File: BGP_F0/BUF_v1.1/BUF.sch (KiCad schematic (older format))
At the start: 35 parts, among them P1 CONN_01X02, P2 CONN_01X02, P3 CONN_01X03, P4 CONN_01X02, P5 CONN_01X09, P6 CONN_01X05, P7 CONN_01X02, Q1 2N5457, Q2 2N5457, U1 MC33178

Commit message: Some changes to names
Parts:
- C6: value 100p -> 270p
- R10: value 100 -> 1k
- R5, R6: value 49.9k -> 47k
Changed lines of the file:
@@
 $EndComp
 $Comp
-L Earth #PWR4
+L Earth #PWR01
 U 1 1 5A651373
 P 2850 2800
-F 0 "#PWR4" H 2850 2550 50  0001 C CNN
+F 0 "#PWR01" H 2850 2550 50  0001 C CNN
 F 1 "Earth" H 2850 2650 50  0001 C CNN
 F 2 "" H 2850 2800 50  0000 C CNN
@@
 VRef
 $Comp
-L Earth #PWR7
+L Earth #PWR02
 U 1 1 5A653AB7
 P 3800 4350
-F 0 "#PWR7" H 3800 4100 50  0001 C CNN
+F 0 "#PWR02" H 3800 4100 50  0001 C CNN
 F 1 "Earth" H 3800 4200 50  0001 C CNN
 F 2 "" H 3800 4350 50  0000 C CNN
@@
 P 5200 2800
 F 0 "R5" H 5230 2820 50  0000 L CNN
-F 1 "49.9k" H 5230 2760 50  0000 L CNN
+F 1 "47k" H 5230 2760 50  0000 L CNN
 F 2 "Resistors_SMD:R_0603" H 5200 2800 50  0001 C CNN
 F 3 "" H 5200 2800 50  0000 C CNN
@@
 P 5200 3200
 F 0 "R6" H 5230 3220 50  0000 L CNN
-F 1 "49.9k" H 5230 3160 50  0000 L CNN
+F 1 "47k" H 5230 3160 50  0000 L CNN
 F 2 "Resistors_SMD:R_0603" H 5200 3200 50  0001 C CNN
 F 3 "" H 5200 3200 50  0000 C CNN
@@
 $EndComp
 $Comp
-L Earth #PWR8
+L Earth #PWR03
 U 1 1 5A654108
 P 5700 3600
-F 0 "#PWR8" H 5700 3350 50  0001 C CNN
+F 0 "#PWR03" H 5700 3350 50  0001 C CNN
 F 1 "Earth" H 5700 3450 50  0001 C CNN
 F 2 "" H 5700 3600 50  0000 C CNN
@@
 P 5700 4100
 F 0 "C6" H 5710 4170 50  0000 L CNN
-F 1 "100p" H 5710 4020 50  0000 L CNN
+F 1 "270p" H 5710 4020 50  0000 L CNN
 F 2 "Capacitors_SMD:C_0603" H 5700 4100 50  0001 C CNN
 F 3 "" H 5700 4100 50  0000 C CNN
@@
 $EndComp
 $Comp
-L Earth #PWR9
+L Earth #PWR04
 U 1 1 5A6549CA
 P 5700 5400
-F 0 "#PWR9" H 5700 5150 50  0001 C CNN
+F 0 "#PWR04" H 5700 5150 50  0001 C CNN
 F 1 "Earth" H 5700 5250 50  0001 C CNN
 F 2 "" H 5700 5400 50  0000 C CNN
@@
 P 7200 3300
 F 0 "R10" H 7230 3320 50  0000 L CNN
-F 1 "100" H 7230 3260 50  0000 L CNN
+F 1 "1k" H 7230 3260 50  0000 L CNN
 F 2 "Resistors_SMD:R_0603" H 7200 3300 50  0001 C CNN
 F 3 "" H 7200 3300 50  0000 C CNN
@@
 $EndComp
 $Comp
-L Earth #PWR10
+L Earth #PWR05
 U 1 1 5A655780
 P 7650 3900
-F 0 "#PWR10" H 7650 3650 50  0001 C CNN
+F 0 "#PWR05" H 7650 3650 50  0001 C CNN
 F 1 "Earth" H 7650 3750 50  0001 C CNN
 F 2 "" H 7650 3900 50  0000 C CNN
@@
 $EndComp
 $Comp
-L Earth #PWR11
+L Earth #PWR06
 U 1 1 5A6578E9
 P 8350 4800
-F 0 "#PWR11" H 8350 4550 50  0001 C CNN
+F 0 "#PWR06" H 8350 4550 50  0001 C CNN
 F 1 "Earth" H 8350 4650 50  0001 C CNN
 F 2 "" H 8350 4800 50  0000 C CNN
@@
 PV_2
 $Comp
-L Earth #PWR2
+L Earth #PWR07
 U 1 1 5A658545
 P 2600 4000
-F 0 "#PWR2" H 2600 3750 50  0001 C CNN
+F 0 "#PWR07" H 2600 3750 50  0001 C CNN
 F 1 "Earth" H 2600 3850 50  0001 C CNN
 F 2 "" H 2600 4000 50  0000 C CNN
@@
 $EndComp
 $Comp
-L Earth #PWR1
+L Earth #PWR08
 U 1 1 5A6585B9
 P 2600 2600
-F 0 "#PWR1" H 2600 2350 50  0001 C CNN
+F 0 "#PWR08" H 2600 2350 50  0001 C CNN
 F 1 "Earth" H 2600 2450 50  0001 C CNN
 F 2 "" H 2600 2600 50  0000 C CNN
@@
 $EndComp
 $Comp
-L Earth #PWR6
+L Earth #PWR09
 U 1 1 5A6514C1
 P 3800 2950
-F 0 "#PWR6" H 3800 2700 50  0001 C CNN
+F 0 "#PWR09" H 3800 2700 50  0001 C CNN
 F 1 "Earth" H 3800 2800 50  0001 C CNN
 F 2 "" H 3800 2950 50  0000 C CNN
@@
 	3500 3900 3250 3900
 $Comp
-L Earth #PWR3
+L Earth #PWR010
 U 1 1 5A65837A
 P 2600 4500
-F 0 "#PWR3" H 2600 4250 50  0001 C CNN
+F 0 "#PWR010" H 2600 4250 50  0001 C CNN
 F 1 "Earth" H 2600 4350 50  0001 C CNN
 F 2 "" H 2600 4500 50  0000 C CNN
@@
 $EndComp
 $Comp
-L Earth #PWR5
+L Earth #PWR011
 U 1 1 5A653A9E
 P 2850 4200
-F 0 "#PWR5" H 2850 3950 50  0001 C CNN
+F 0 "#PWR011" H 2850 3950 50  0001 C CNN
 F 1 "Earth" H 2850 4050 50  0001 C CNN
 F 2 "" H 2850 4200 50  0000 C CNN

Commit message: F0 BUF changed rotation
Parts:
- removed P5: CONN_01X09, LIBS:Potentiometer_Alpha_Tripple_Vertical_Dual_Shaft, symbol CONN_01X09
- removed P7: CONN_01X02, Connectors_JST:JST_PH_B2B-PH-K_02x2.00mm_Straight, symbol CONN_01X02
- added P5: Conn_01x06, LIBS:Potentiometer_Alpha_Double_Vertical_Dual_Shaft, symbol Conn_01x06
- added R18: 12k, Resistors_SMD:R_0603, symbol R_Small
- R11: value 10k -> 20k
- R5, R6: value 47k -> 4.7k
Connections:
- net labels added: PB2_1
- net labels removed: PB2_3, PV_1, PV_3
- wire segments 52 -> 57
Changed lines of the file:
@@
 $EndComp
 $Comp
-L Earth #PWR01
+L Earth #PWR4
 U 1 1 5A651373
 P 2850 2800
-F 0 "#PWR01" H 2850 2550 50  0001 C CNN
+F 0 "#PWR4" H 2850 2550 50  0001 C CNN
 F 1 "Earth" H 2850 2650 50  0001 C CNN
 F 2 "" H 2850 2800 50  0000 C CNN
@@
 VRef
 $Comp
-L Earth #PWR02
+L Earth #PWR7
 U 1 1 5A653AB7
 P 3800 4350
-F 0 "#PWR02" H 3800 4100 50  0001 C CNN
+F 0 "#PWR7" H 3800 4100 50  0001 C CNN
 F 1 "Earth" H 3800 4200 50  0001 C CNN
 F 2 "" H 3800 4350 50  0000 C CNN
@@
 P 5200 2800
 F 0 "R5" H 5230 2820 50  0000 L CNN
-F 1 "47k" H 5230 2760 50  0000 L CNN
+F 1 "4.7k" H 5230 2760 50  0000 L CNN
 F 2 "Resistors_SMD:R_0603" H 5200 2800 50  0001 C CNN
 F 3 "" H 5200 2800 50  0000 C CNN
@@
 P 5200 3200
 F 0 "R6" H 5230 3220 50  0000 L CNN
-F 1 "47k" H 5230 3160 50  0000 L CNN
+F 1 "4.7k" H 5230 3160 50  0000 L CNN
 F 2 "Resistors_SMD:R_0603" H 5200 3200 50  0001 C CNN
 F 3 "" H 5200 3200 50  0000 C CNN
@@
 $EndComp
 $Comp
-L Earth #PWR03
+L Earth #PWR8
 U 1 1 5A654108
 P 5700 3600
-F 0 "#PWR03" H 5700 3350 50  0001 C CNN
+F 0 "#PWR8" H 5700 3350 50  0001 C CNN
 F 1 "Earth" H 5700 3450 50  0001 C CNN
 F 2 "" H 5700 3600 50  0000 C CNN
@@
 $EndComp
 $Comp
-L Earth #PWR04
+L Earth #PWR9
 U 1 1 5A6549CA
 P 5700 5400
-F 0 "#PWR04" H 5700 5150 50  0001 C CNN
+F 0 "#PWR9" H 5700 5150 50  0001 C CNN
 F 1 "Earth" H 5700 5250 50  0001 C CNN
 F 2 "" H 5700 5400 50  0000 C CNN
@@
 PB2_2
 Text Label 4550 3300 0    60   ~ 0
-PB2_3
+PB2_1
 $Comp
 L R_Small R11
@@
 P 7650 3450
 F 0 "R11" H 7680 3470 50  0000 L CNN
-F 1 "10k" H 7680 3410 50  0000 L CNN
+F 1 "20k" H 7680 3410 50  0000 L CNN
 F 2 "Resistors_SMD:R_0603" H 7650 3450 50  0001 C CNN
 F 3 "" H 7650 3450 50  0000 C CNN
@@
 $EndComp
 $Comp
-L R_Small R12
-U 1 1 5A655616
-P 7650 3750
-F 0 "R12" H 7680 3770 50  0000 L CNN
-F 1 "12k" H 7680 3710 50  0000 L CNN
-F 2 "Resistors_SMD:R_0603" H 7650 3750 50  0001 C CNN
-F 3 "" H 7650 3750 50  0000 C CNN
-	1    7650 3750
-	1    0    0    -1
-$EndComp
-$Comp
-L Earth #PWR05
+L Earth #PWR10
 U 1 1 5A655780
-P 7650 3900
-F 0 "#PWR05" H 7650 3650 50  0001 C CNN
-F 1 "Earth" H 7650 3750 50  0001 C CNN
-F 2 "" H 7650 3900 50  0000 C CNN
-F 3 "" H 7650 3900 50  0000 C CNN
-	1    7650 3900
-	1    0    0    -1
-$EndComp
-Text Label 7650 3900 0    60   ~ 0
-PV_1
-Text Label 7650 3650 0    60   ~ 0
-PV_2
-Text Label 7650 3350 0    60   ~ 0
-PV_3
+P 7650 3600
+F 0 "#PWR10" H 7650 3350 50  0001 C CNN
+F 1 "Earth" H 7650 3450 50  0001 C CNN
+F 2 "" H 7650 3600 50  0000 C CNN
+F 3 "" H 7650 3600 50  0000 C CNN
+	1    7650 3600
+	1    0    0    -1
+$EndComp
 Text Label 7100 3300 2    60   ~ 0
 OUT_EQ
@@
 Text Label 2600 3900 0    60   ~ 0
 IN_B
-$Comp
-L CONN_01X09 P5
-U 1 1 5A656FFD
-P 8550 3750
-F 0 "P5" H 8550 4250 50  0000 C CNN
-F 1 "CONN_01X09" V 8650 3750 50  0000 C CNN
-F 2 "LIBS:Potentiometer_Alpha_Tripple_Vertical_Dual_Shaft" H 8550 3750 50  0001 C CNN
-F 3 "" H 8550 3750 50  0000 C CNN
-	1    8550 3750
-	1    0    0    -1
-$EndComp
-Text Label 8350 4150 2    60   ~ 0
-PV_3
-Text Label 8950 3450 2    60   ~ 0
-PV_3
-Text Label 8350 4050 2    60   ~ 0
-PV_2
-Text Label 8350 3950 2    60   ~ 0
-PV_1
-Text Label 8950 3350 2    60   ~ 0
-PV_1
-Text Label 8350 3350 2    60   ~ 0
+Text Label 8350 3550 2    60   ~ 0
 PB1_1
 Text Label 8350 3450 2    60   ~ 0
@@
 Text Label 8350 3750 2    60   ~ 0
 PB2_2
-Text Label 8350 3850 2    60   ~ 0
-PB2_3
 $Comp
 L CONN_01X05 P6
@@
 $EndComp
 $Comp
-L Earth #PWR06
+L Earth #PWR11
 U 1 1 5A6578E9
 P 8350 4800
-F 0 "#PWR06" H 8350 4550 50  0001 C CNN
+F 0 "#PWR11" H 8350 4550 50  0001 C CNN
 F 1 "Earth" H 8350 4650 50  0001 C CNN
 F 2 "" H 8350 4800 50  0000 C CNN
@@
 PV_2
 $Comp
-L Earth #PWR07
+L Earth #PWR2
 U 1 1 5A658545
 P 2600 4000
-F 0 "#PWR07" H 2600 3750 50  0001 C CNN
+F 0 "#PWR2" H 2600 3750 50  0001 C CNN
 F 1 "Earth" H 2600 3850 50  0001 C CNN
 F 2 "" H 2600 4000 50  0000 C CNN
@@
 $EndComp
 $Comp
-L Earth #PWR08
+L Earth #PWR1
 U 1 1 5A6585B9
 P 2600 2600
-F 0 "#PWR08" H 2600 2350 50  0001 C CNN
+F 0 "#PWR1" H 2600 2350 50  0001 C CNN
 F 1 "Earth" H 2600 2450 50  0001 C CNN
 F 2 "" H 2600 2600 50  0000 C CNN
@@
 $EndComp
 $Comp
-L Earth #PWR09
+L Earth #PWR6
 U 1 1 5A6514C1
 P 3800 2950
-F 0 "#PWR09" H 3800 2700 50  0001 C CNN
+F 0 "#PWR6" H 3800 2700 50  0001 C CNN
 F 1 "Earth" H 3800 2800 50  0001 C CNN
 F 2 "" H 3800 2950 50  0000 C CNN
@@
 	2600 5050 2600 4700
 Wire Wire Line
-	8350 3550 8350 3650
-Wire Wire Line
 	7100 3300 6750 3300
 Wire Wire Line
@@
 Wire Wire Line
 	7550 3300 7650 3300
-Wire Wire Line
-	7650 3650 7650 3550
-Wire Wire Line
-	7650 3900 7650 3850
 Wire Wire Line
 	7300 3300 7350 3300
@@
 	3500 3900 3250 3900
 $Comp
-L Earth #PWR010
+L Earth #PWR3
 U 1 1 5A65837A
 P 2600 4500
-F 0 "#PWR010" H 2600 4250 50  0001 C CNN
+F 0 "#PWR3" H 2600 4250 50  0001 C CNN
 F 1 "Earth" H 2600 4350 50  0001 C CNN
 F 2 "" H 2600 4500 50  0000 C CNN
@@
 $EndComp
 $Comp
-L Earth #PWR011
+L Earth #PWR5
 U 1 1 5A653A9E
 P 2850 4200
-F 0 "#PWR011" H 2850 3950 50  0001 C CNN
+F 0 "#PWR5" H 2850 3950 50  0001 C CNN
 F 1 "Earth" H 2850 4050 50  0001 C CNN
 F 2 "" H 2850 4200 50  0000 C CNN
@@
 $EndComp
 $Comp
-L CONN_01X02 P7
-U 1 1 5A7A3189
-P 9150 3400
-F 0 "P7" H 9150 3550 50  0000 C CNN
-F 1 "CONN_01X02" V 9250 3400 50  0000 C CNN
-F 2 "Connectors_JST:JST_PH_B2B-PH-K_02x2.00mm_Straight" H 9150 3400 50  0001 C CNN
-F 3 "" H 9150 3400 50  0000 C CNN
-	1    9150 3400
-	1    0    0    -1
-$EndComp
-$Comp
 L R_Small R13
 U 1 1 5A7A4415
@@
 	5400 2800 5300 2800
 Connection ~ 5400 3200
+$Comp
+L Conn_01x06 P5
+U 1 1 5AF59195
+P 8550 3550
+F 0 "P5" H 8550 3850 50  0000 C CNN
+F 1 "Conn_01x06" H 8550 3150 50  0000 C CNN
+F 2 "LIBS:Potentiometer_Alpha_Double_Vertical_Dual_Shaft" H 8550 3550 50  0001 C CNN
+F 3 "" H 8550 3550 50  0001 C CNN
+	1    8550 3550
+	1    0    0    -1
+$EndComp
+Wire Wire Line
+	7650 3600 7650 3550
+Text Label 8350 3850 2    60   ~ 0
+PB2_1
+Text Label 8350 3350 2    60   ~ 0
+VRef
+$Comp
+L R_Small R18
+U 1 1 5AF597CB
+P 4750 3350
+F 0 "R18" H 4780 3370 50  0000 L CNN
+F 1 "12k" H 4780 3310 50  0000 L CNN
+F 2 "Resistors_SMD:R_0603" H 4750 3350 50  0001 C CNN
+F 3 "" H 4750 3350 50  0000 C CNN
+	1    4750 3350
+	0    1    1    0
+$EndComp
+$Comp
+L R_Small R12
+U 1 1 5AF59855
+P 4750 2900
+F 0 "R12" H 4780 2920 50  0000 L CNN
+F 1 "12k" H 4780 2860 50  0000 L CNN
+F 2 "Resistors_SMD:R_0603" H 4750 2900 50  0001 C CNN
+F 3 "" H 4750 2900 50  0000 C CNN
+	1    4750 2900
+	0    1    1    0
+$EndComp
+Wire Wire Line
+	4650 2900 4550 2900
+Wire Wire Line
+	4550 2900 4550 2700
+Wire Wire Line
+	4850 2900 5000 2900
+Wire Wire Line
+	5000 2900 5000 2800
+Wire Wire Line
+	4550 3350 4650 3350
+Connection ~ 4550 3350
+Wire Wire Line
+	4850 3350 5000 3350
+Wire Wire Line
+	5000 3350 5000 3200
 $EndSCHEMATC

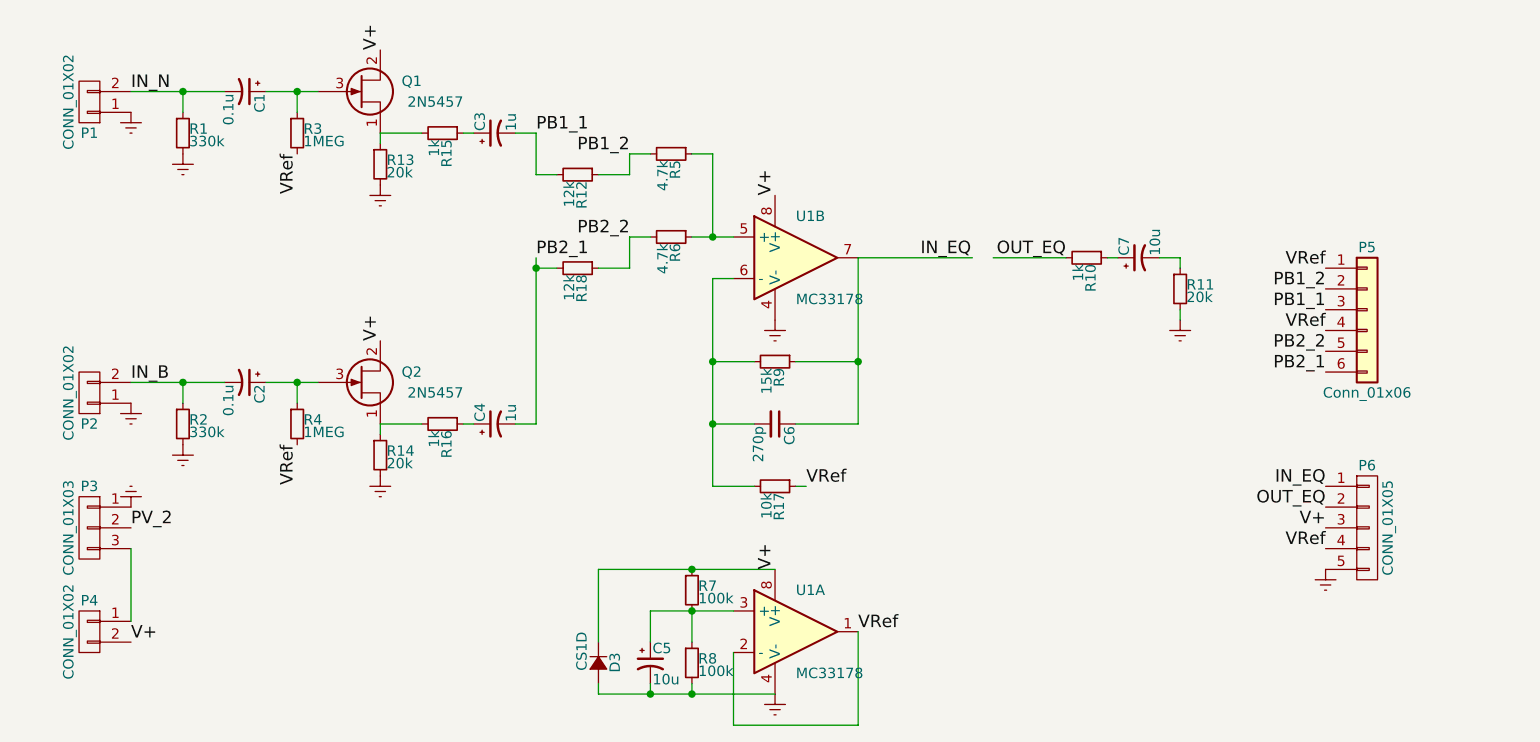
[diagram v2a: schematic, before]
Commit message: Tone Pot connector and output routing added
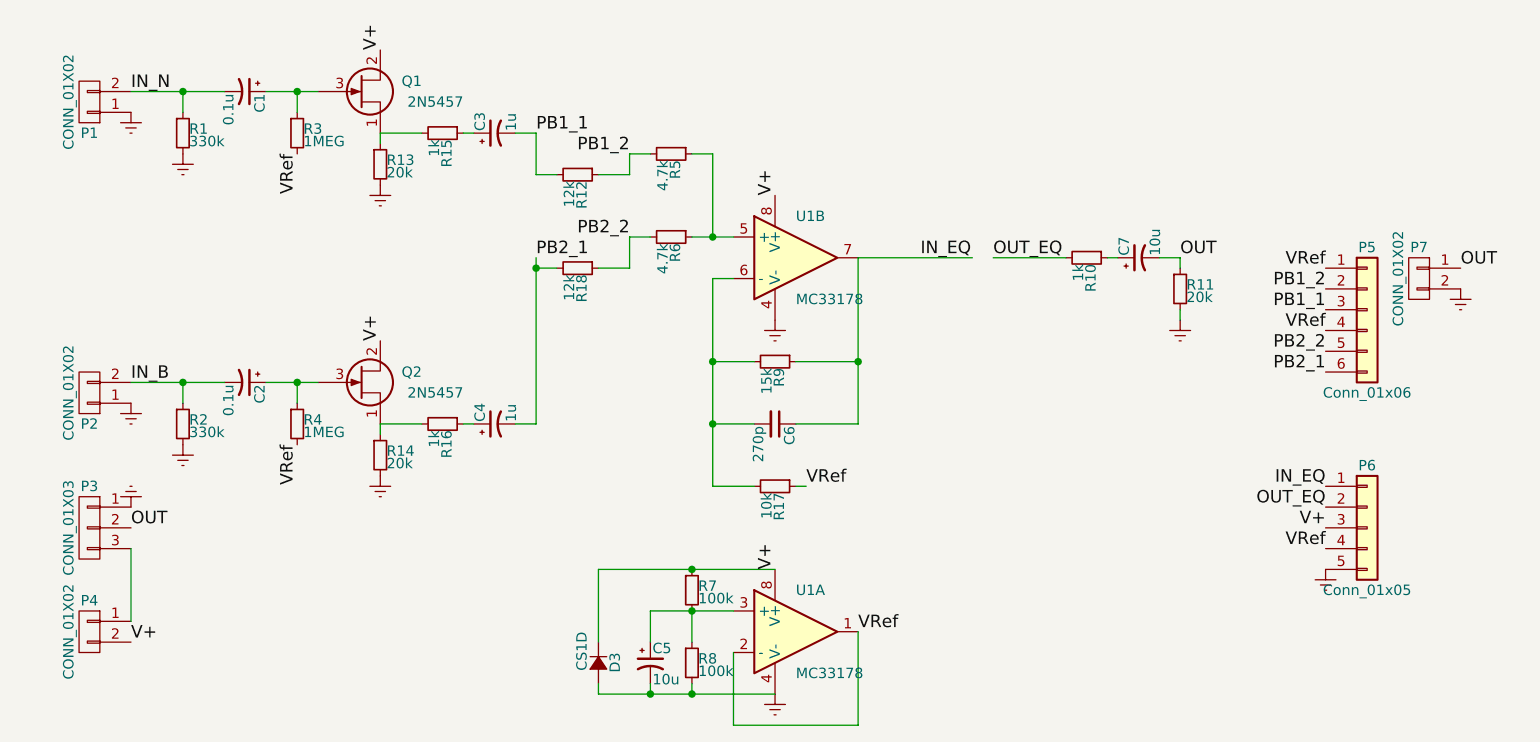
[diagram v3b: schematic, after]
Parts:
- removed P6: CONN_01X05, Connectors_JST:JST_PH_B5B-PH-K_05x2.00mm_Straight, symbol CONN_01X05
- added P6: Conn_01x05, Connectors_JST:JST_PH_B5B-PH-K_05x2.00mm_Straight, symbol Conn_01x05
- added P7: CONN_01X02, Connectors_JST:JST_PH_B2B-PH-K_02x2.00mm_Straight, symbol CONN_01X02
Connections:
- net labels added: OUT
- net labels removed: PV_2

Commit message: F0 Vol/Vol spec LOG pots
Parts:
- removed R12, R18: 12k, Resistors_SMD:R_0603, symbol R_Small
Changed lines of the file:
@@
 VRef
-$Comp
-L R_Small R18
-U 1 1 5AF597CB
-P 4750 3350
-F 0 "R18" H 4780 3370 50  0000 L CNN
-F 1 "12k" H 4780 3310 50  0000 L CNN
-F 2 "Resistors_SMD:R_0603" H 4750 3350 50  0001 C CNN
-F 3 "" H 4750 3350 50  0000 C CNN
-	1    4750 3350
-	0    1    1    0
-$EndComp
-$Comp
-L R_Small R12
-U 1 1 5AF59855
-P 4750 2900
-F 0 "R12" H 4780 2920 50  0000 L CNN
-F 1 "12k" H 4780 2860 50  0000 L CNN
-F 2 "Resistors_SMD:R_0603" H 4750 2900 50  0001 C CNN
-F 3 "" H 4750 2900 50  0000 C CNN
-	1    4750 2900
-	0    1    1    0
-$EndComp
-Wire Wire Line
-	4650 2900 4550 2900
-Wire Wire Line
-	4550 2900 4550 2700
-Wire Wire Line
-	4850 2900 5000 2900
-Wire Wire Line
-	5000 2900 5000 2800
-Wire Wire Line
-	4550 3350 4650 3350
-Connection ~ 4550 3350
-Wire Wire Line
-	4850 3350 5000 3350
-Wire Wire Line
-	5000 3350 5000 3200
 $Comp
 L Conn_01x05 P6
